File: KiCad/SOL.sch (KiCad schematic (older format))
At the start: 4 parts

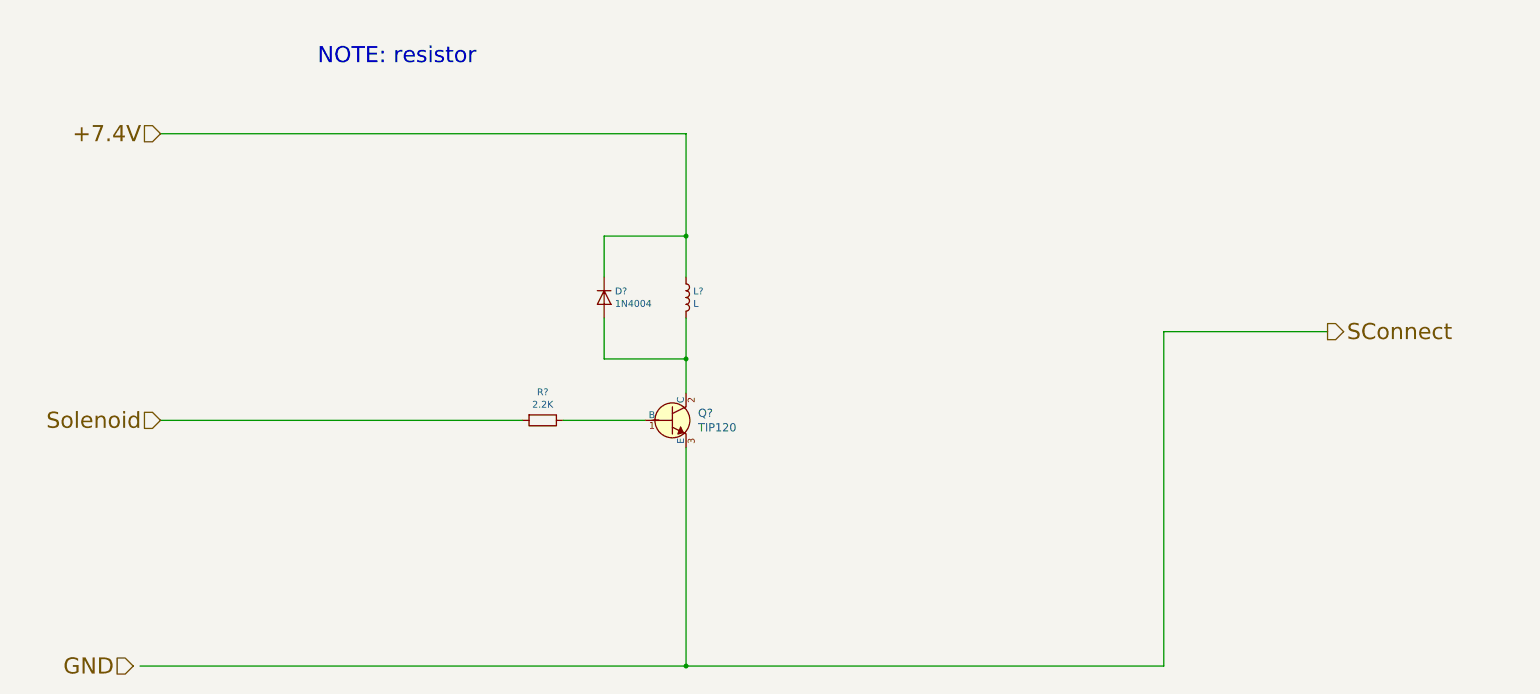
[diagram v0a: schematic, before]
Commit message: add solenoid circuit
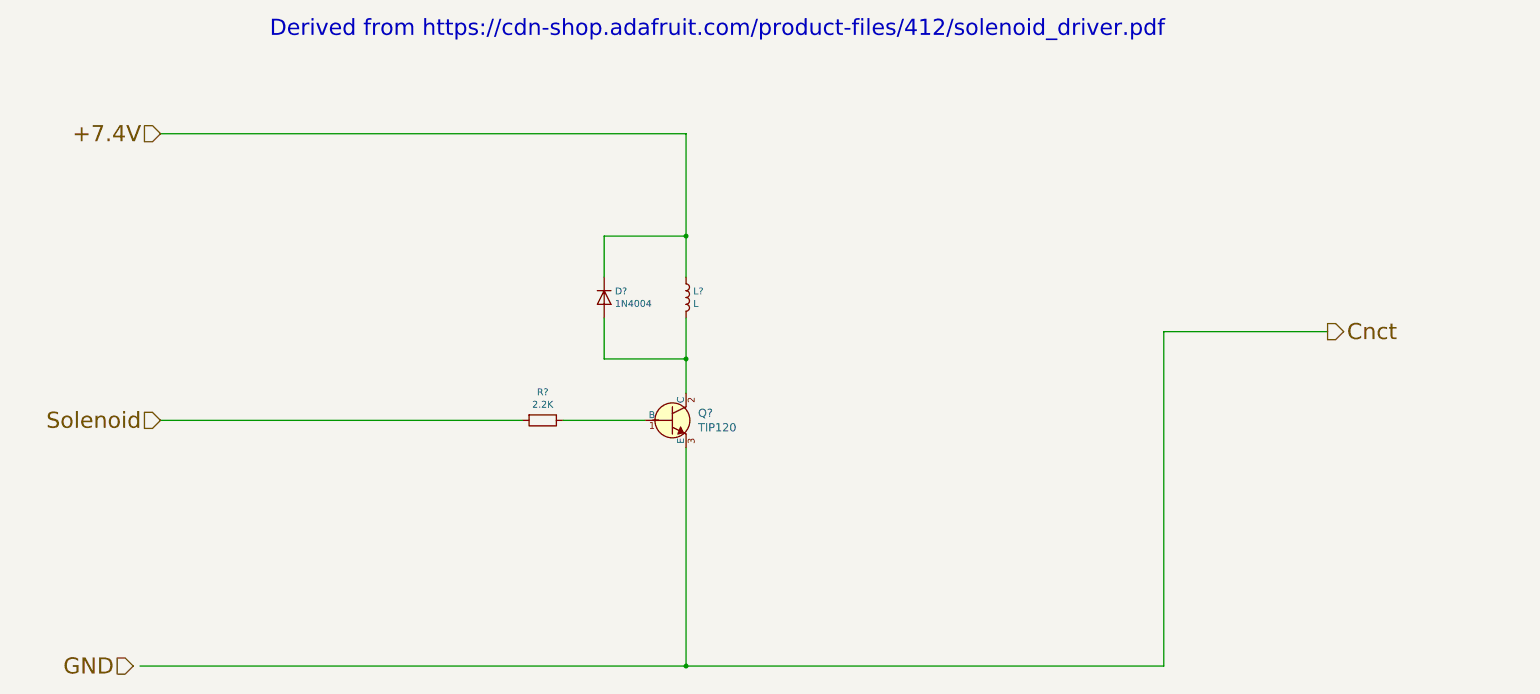
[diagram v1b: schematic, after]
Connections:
- net labels added: Cnct
- net labels removed: SConnect
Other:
- note added: "Derived from https://cdn-shop.adafruit.com/product-files/412/solenoid_driver.pdf"
- note removed: "NOTE: resistor"
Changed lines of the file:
@@
 Sheet 2 2
 Title "Rubber Band Gun"
-Date "2019-09-13"
+Date "2020-03-20"
 Rev "---"
 Comp ""
-Comment1 ""
+Comment1 "Solenoid Circuit"
 Comment2 ""
 Comment3 ""
@@
 Solenoid
 Text HLabel 10150 3500 2    118  Output ~ 0
-SConnect
+Cnct
 $Comp
 L dk_Transistors-Bipolar-BJT-Single:TIP120 Q?
@@
 	1    0    0    -1
 $EndComp
-Text Notes 2750 1550 0    118  ~ 0
-NOTE: resistor
 Wire Wire Line
 	1600 2050 5450 2050
@@
 Wire Wire Line
 	4250 4150 1600 4150
+Text Notes 2400 1350 0    118  ~ 0
+Derived from https://cdn-shop.adafruit.com/product-files/412/solenoid_driver.pdf
 $EndSCHEMATC
